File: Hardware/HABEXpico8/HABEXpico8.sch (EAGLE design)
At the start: 121 parts, among them IC1 LT1763CS8-3.3, Q1 2.5A/30V, SW1 SKQGADE010, SW2 SKQGADE010, U1 LTC3106, U2 EVA-8M, U3 STM32L011G4, U4 SI4464, U5 USB-C_R/A_HYBRID_RCPT, U6 FT232RL, U7 3.3V, X1 BU-SMA-V, X2 BU-SMA-V, X3 BU-SMA-V, X4 BU-SMA-V, X5 JTI_ANTENNA-1575AT43A40, X6 C-GRID-04-70553, X7 C-GRID-02-70553, X8 30MHZ 402F3001XIAR, X9 BU-SMA-V, Y1 ABS07-120-32.768KHZ-T, Y2 ABS07-120-32.768KHZ-T

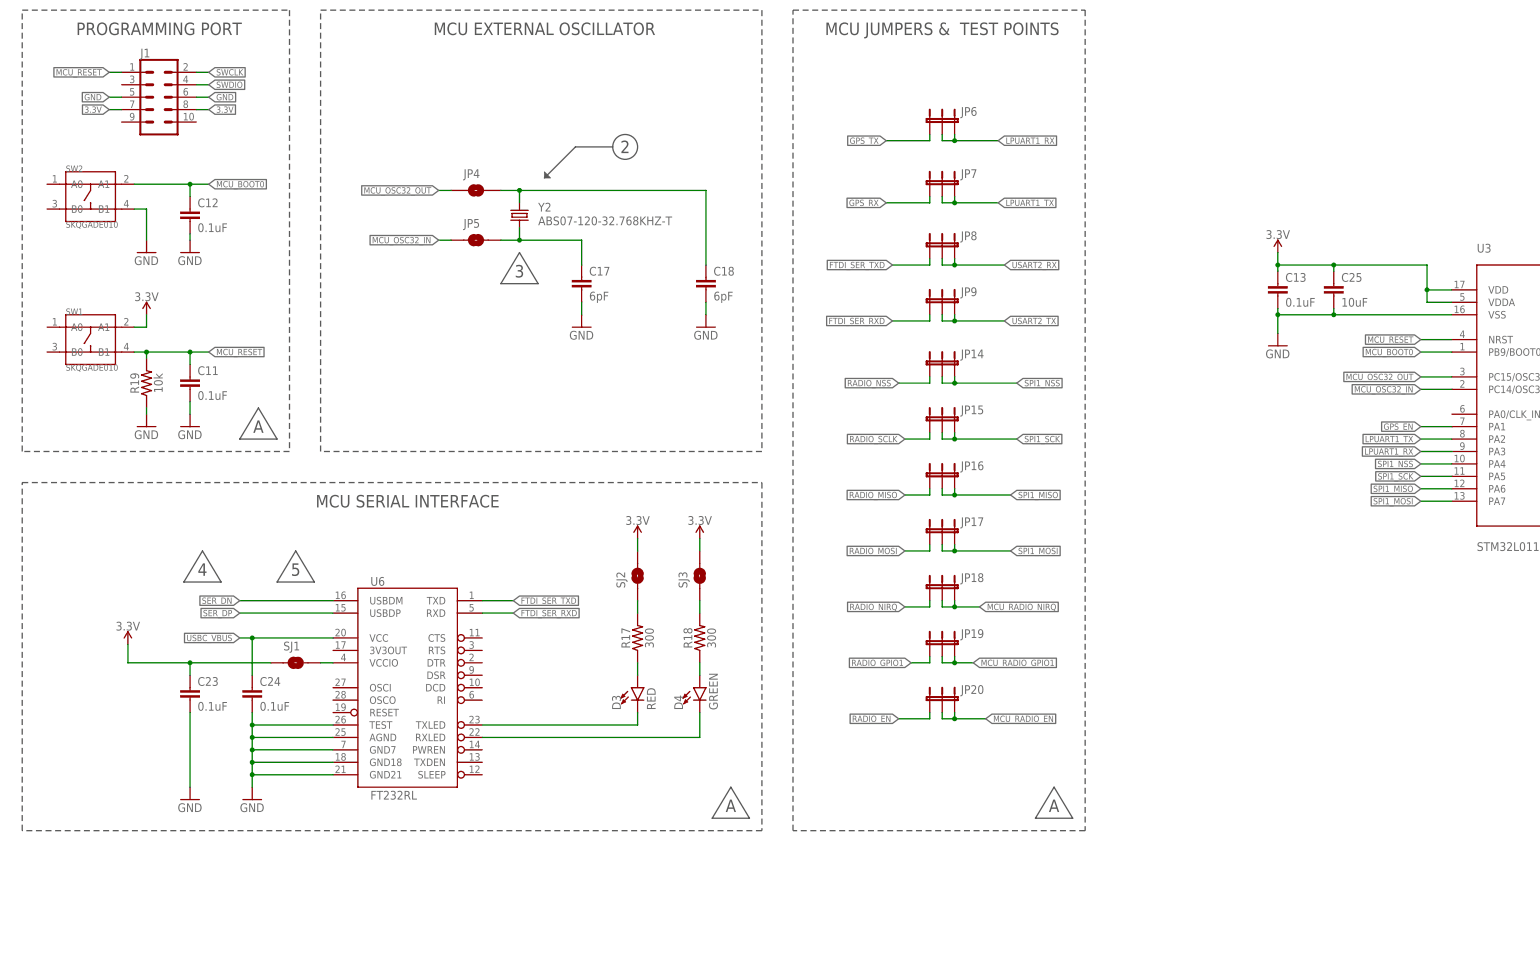
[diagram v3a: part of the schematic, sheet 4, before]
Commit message: Added BOM, updated board/schematic files
Added BOM, updated board/schematic files
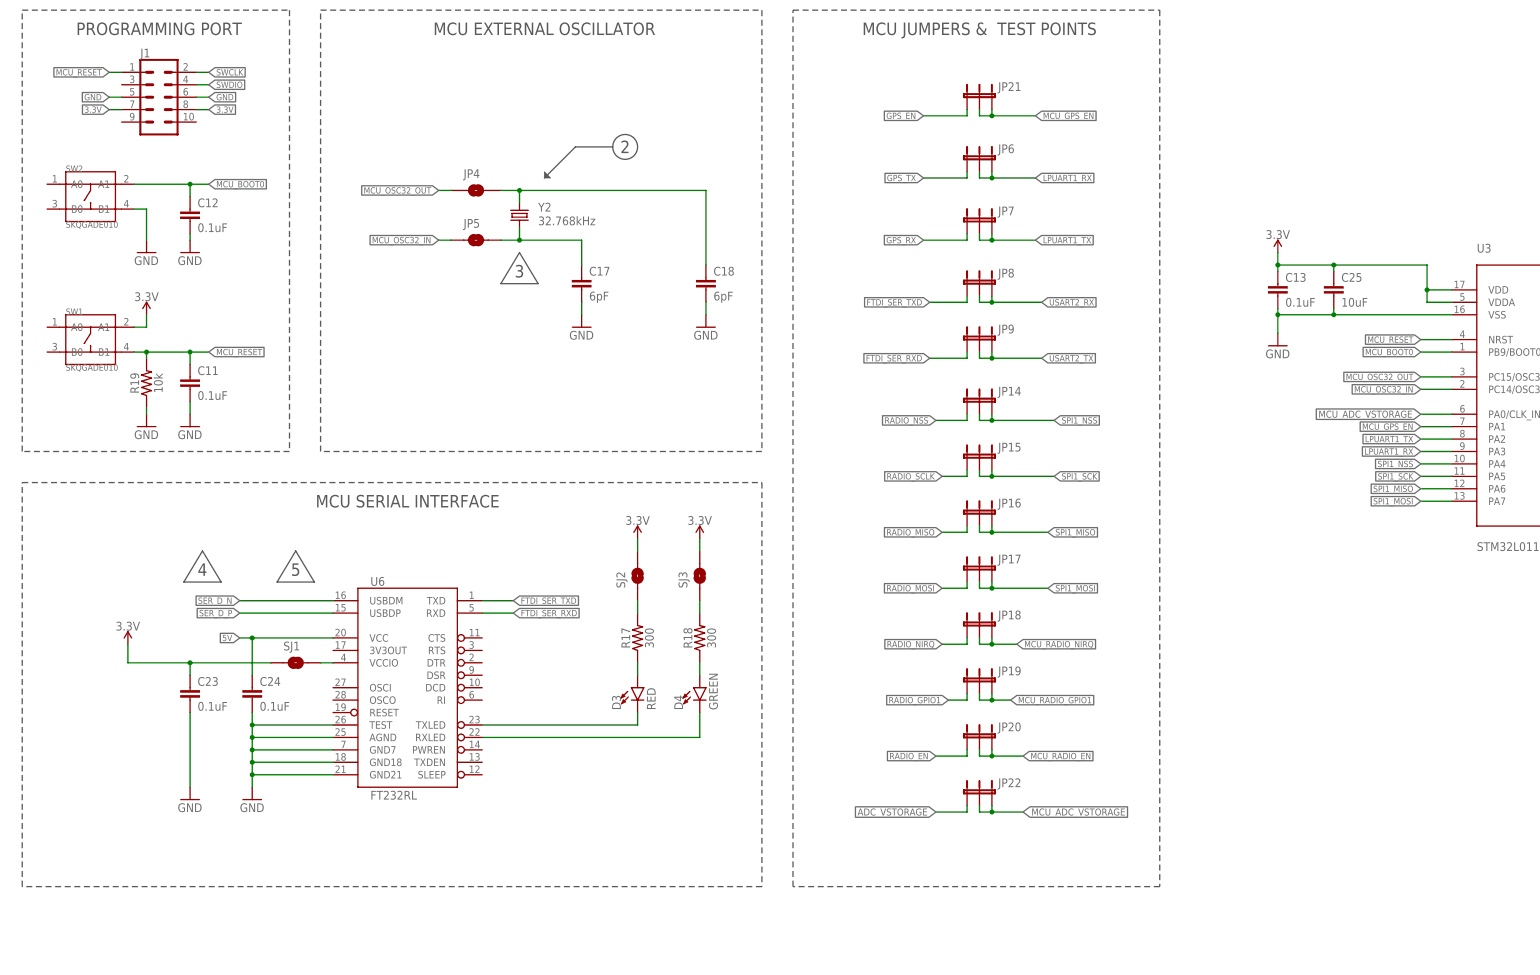
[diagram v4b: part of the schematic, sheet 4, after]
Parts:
- added JP21, JP22: JUMPER-3PTH, SparkFun-Retired:JUMPER-3PTH
- R1, R9: value 2.21M -> 1M
- R10, R2: value 1.33M -> 1M
- R14, R15: value 5.1k 10% -> 5.1K
- R3: value 10M -> 1M
- Y1, Y2: value ABS07-120-32.768KHZ-T -> 32.768kHz
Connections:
- net GPS_USB_DM renamed GPS_USB_N
- net GPS_USB_DP renamed GPS_USB_P
- net SER_DN renamed SER_D_N
- net SER_DP renamed SER_D_P
- new net ADC_VSTORAGE: JP22.1, R10.2, R9.1
- new net MCU_GPS_EN: JP21.2, JP21.3, U3.PA1
- net 5V: now also C24.1, U6.VCC
- net GPS_EN: now also JP21.1; no longer U3.PA1
- net MCU_ADC_VSTORAGE: now also JP22.2, JP22.3, U3.PA0/CLK_IN; no longer R10.2, R9.1
- net N$15: now also R16.1; no longer R13.1
- net N$16: now also R13.1; no longer R16.1
- net USBC_DN: now also CR2.I/O2_2; no longer CR2.I/O1_2
- net USBC_DP: now also CR2.I/O1_2; no longer CR2.I/O2_2
- net USBC_VBUS: no longer C24.1, U6.VCC
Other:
- note added: "1. BOARD DESIGN FOR PROGRAMMING, TESTING, AND QUALIFYING DEVICES NOTES: THIS PAGE"
- note added: "3.3V REGULATOR"
- note removed: "5V REGULATOR"
- note removed: "SUPPORT HARDWARE, NOT FOR FLIGHT 1. BOARD DESIGN FOR PROGRAMMING, TESTING, AND QUALIFYING DEVICES NOTES: THIS PAGE"
- moved on the sheet: JP14, JP15, JP16, JP17, JP18, JP19, JP20, JP6, JP7, JP8, JP9, R13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

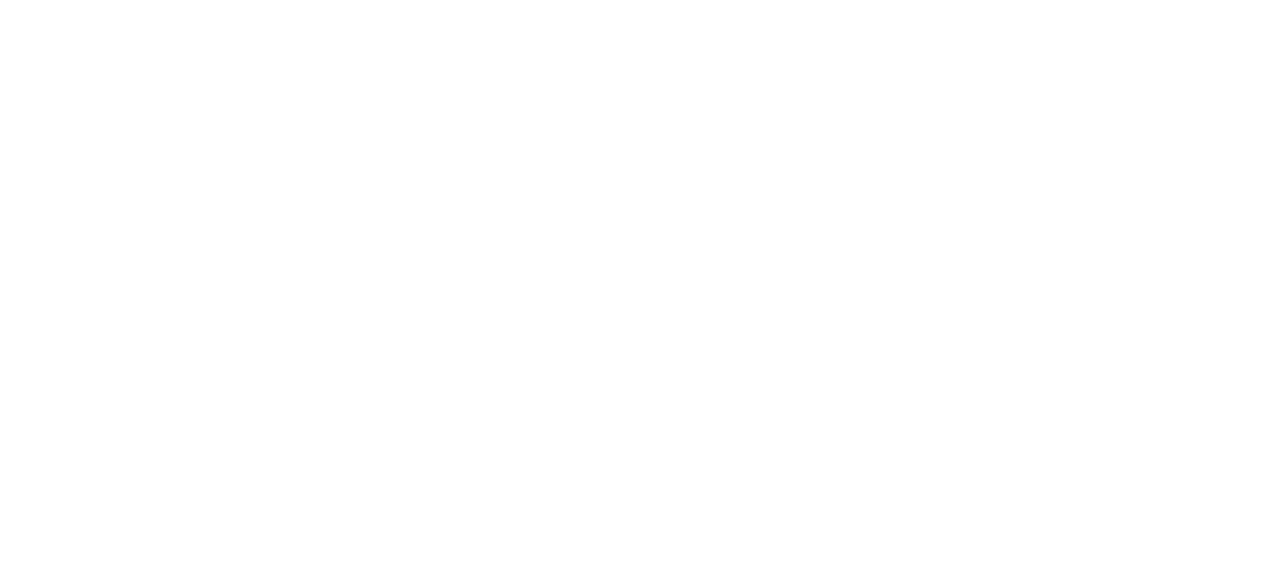
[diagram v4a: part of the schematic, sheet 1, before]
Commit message: Updated project to use the new stm32l0xx-hal
Updated project to use the new stm32l0xx-hal
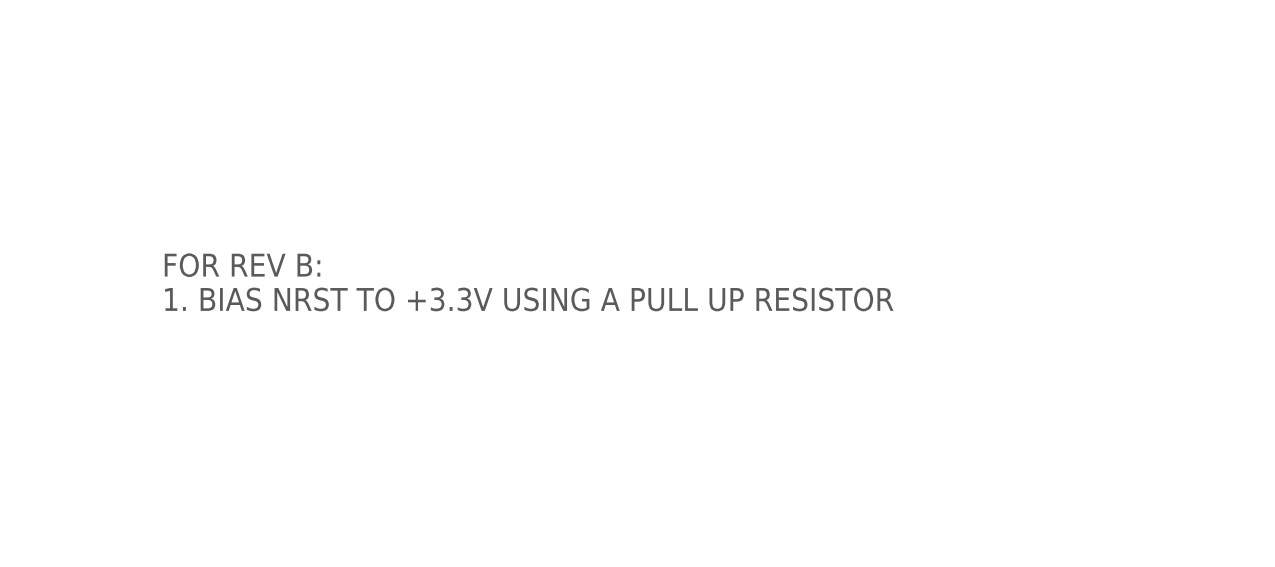
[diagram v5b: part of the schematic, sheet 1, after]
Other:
- note added: "FOR REV B: 1. BIAS NRST TO +3.3V USING A PULL UP RESISTOR"
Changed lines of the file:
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@@
 <?xml version="1.0" encoding="utf-8"?>
 <!DOCTYPE eagle SYSTEM "eagle.dtd">
-<eagle version="9.1.2">
+<eagle version="9.1.3">
 <drawing>
 <settings>
@@
 <setting verticaltext="up"/>
 </settings>
-<grid distance="0.05" unitdist="inch" unit="inch" style="dots" multiple="1" display="yes" altdistance="0.01" altunitdist="inch" altunit="inch"/>
+<grid distance="0.1" unitdist="inch" unit="inch" style="lines" multiple="1" display="no" altdistance="0.01" altunitdist="inch" altunit="inch"/>
 <layers>
-<layer number="1" name="Top" color="4" fill="1" visible="yes" active="no"/>
-<layer number="2" name="Route2" color="1" fill="3" visible="yes" active="no"/>
-<layer number="3" name="Route3" color="4" fill="3" visible="yes" active="no"/>
-<layer number="4" name="Route4" color="1" fill="4" visible="yes" active="no"/>
-<layer number="5" name="Route5" color="4" fill="4" visible="yes" active="no"/>
-<layer number="6" name="Route6" color="1" fill="8" visible="yes" active="no"/>
-<layer number="7" name="Route7" color="4" fill="8" visible="yes" active="no"/>
-<layer number="8" name="Route8" color="1" fill="2" visible="yes" active="no"/>
-<layer number="9" name="Route9" color="4" fill="2" visible="yes" active="no"/>
-<layer number="10" name="Route10" color="1" fill="7" visible="yes" active="no"/>
-<layer number="11" name="Route11" color="4" fill="7" visible="yes" active="no"/>
-<layer number="12" name="Route12" color="1" fill="5" visible="yes" active="no"/>
-<layer number="13" name="Route13" color="4" fill="5" visible="yes" active="no"/>
-<layer number="14" name="Route14" color="1" fill="6" visible="yes" active="no"/>
-<layer number="15" name="Route15" color="4" fill="6" visible="yes" active="no"/>
-<layer number="16" name="Bottom" color="1" fill="1" visible="yes" active="no"/>
-<layer number="17" name="Pads" color="2" fill="1" visible="yes" active="no"/>
-<layer number="18" name="Vias" color="2" fill="1" visible="yes" active="no"/>
-<layer number="19" name="Unrouted" color="6" fill="1" visible="yes" active="no"/>
-<layer number="20" name="Dimension" color="24" fill="1" visible="yes" active="no"/>
-<layer number="21" name="tPlace" color="7" fill="1" visible="yes" active="no"/>
-<layer number="22" name="bPlace" color="7" fill="1" visible="yes" active="no"/>
-<layer number="23" name="tOrigins" color="15" fill="1" visible="yes" active="no"/>
-<layer number="24" name="bOrigins" color="15" fill="1" visible="yes" active="no"/>
-<layer number="25" name="tNames" color="7" fill="1" visible="yes" active="no"/>
-<layer number="26" name="bNames" color="7" fill="1" visible="yes" active="no"/>
-<layer number="27" name="tValues" color="7" fill="1" visible="yes" active="no"/>
-<layer number="28" name="bValues" color="7" fill="1" visible="yes" active="no"/>
+<layer number="1" name="Top" color="4" fill="1" visible="no" active="no"/>
+<layer number="2" name="Route2" color="1" fill="3" visible="no" active="no"/>
+<layer number="3" name="Route3" color="4" fill="3" visible="no" active="no"/>
+<layer number="4" name="Route4" color="1" fill="4" visible="no" active="no"/>
+<layer number="5" name="Route5" color="4" fill="4" visible="no" active="no"/>
+<layer number="6" name="Route6" color="1" fill="8" visible="no" active="no"/>
+<layer number="7" name="Route7" color="4" fill="8" visible="no" active="no"/>
+<layer number="8" name="Route8" color="1" fill="2" visible="no" active="no"/>
+<layer number="9" name="Route9" color="4" fill="2" visible="no" active="no"/>
+<layer number="10" name="Route10" color="1" fill="7" visible="no" active="no"/>
+<layer number="11" name="Route11" color="4" fill="7" visible="no" active="no"/>
+<layer number="12" name="Route12" color="1" fill="5" visible="no" active="no"/>
+<layer number="13" name="Route13" color="4" fill="5" visible="no" active="no"/>
+<layer number="14" name="Route14" color="1" fill="6" visible="no" active="no"/>
+<layer number="15" name="Route15" color="4" fill="6" visible="no" active="no"/>
+<layer number="16" name="Bottom" color="1" fill="1" visible="no" active="no"/>
+<layer number="17" name="Pads" color="2" fill="1" visible="no" active="no"/>
+<layer number="18" name="Vias" color="2" fill="1" visible="no" active="no"/>
+<layer number="19" name="Unrouted" color="6" fill="1" visible="no" active="no"/>
+<layer number="20" name="Dimension" color="24" fill="1" visible="no" active="no"/>
+<layer number="21" name="tPlace" color="7" fill="1" visible="no" active="no"/>
+<layer number="22" name="bPlace" color="7" fill="1" visible="no" active="no"/>
+<layer number="23" name="tOrigins" color="15" fill="1" visible="no" active="no"/>
+<layer number="24" name="bOrigins" color="15" fill="1" visible="no" active="no"/>
+<layer number="25" name="tNames" color="7" fill="1" visible="no" active="no"/>
+<layer number="26" name="bNames" color="7" fill="1" visible="no" active="no"/>
+<layer number="27" name="tValues" color="7" fill="1" visible="no" active="no"/>
+<layer number="28" name="bValues" color="7" fill="1" visible="no" active="no"/>
 <layer number="29" name="tStop" color="7" fill="3" visible="no" active="no"/>
 <layer number="30" name="bStop" color="7" fill="6" visible="no" active="no"/>
@@
 <layer number="35" name="tGlue" color="7" fill="4" visible="no" active="no"/>
 <layer number="36" name="bGlue" color="7" fill="5" visible="no" active="no"/>
-<layer number="37" name="tTest" color="7" fill="1" visible="yes" active="no"/>
-<layer number="38" name="bTest" color="7" fill="1" visible="yes" active="no"/>
+<layer number="37" name="tTest" color="7" fill="1" visible="no" active="no"/>
+<layer number="38" name="bTest" color="7" fill="1" visible="no" active="no"/>
 <layer number="39" name="tKeepout" color="4" fill="11" visible="no" active="no"/>
 <layer number="40" name="bKeepout" color="1" fill="11" visible="no" active="no"/>
@@
 <layer number="44" name="Drills" color="7" fill="1" visible="no" active="no"/>
 <layer number="45" name="Holes" color="7" fill="1" visible="no" active="no"/>
-<layer number="46" name="Milling" color="3" fill="1" visible="yes" active="no"/>
-<layer number="47" name="Measures" color="7" fill="1" visible="yes" active="no"/>
-<layer number="48" name="Document" color="7" fill="1" visible="yes" active="no"/>
-<layer number="49" name="Reference" color="7" fill="1" visible="yes" active="no"/>
-<layer number="50" name="dxf" color="7" fill="1" visible="yes" active="no"/>
-<layer number="51" name="tDocu" color="7" fill="1" visible="yes" active="no"/>
-<layer number="52" name="bDocu" color="7" fill="1" visible="yes" active="no"/>
-<layer number="53" name="tGND_GNDA" color="7" fill="9" visible="yes" active="no"/>
-<layer number="54" name="bGND_GNDA" color="1" fill="9" visible="yes" active="no"/>
-<layer number="56" name="wert" color="7" fill="1" visible="yes" active="no"/>
-<layer number="57" name="tCAD" color="7" fill="1" visible="yes" active="no"/>
-<layer number="59" name="tCarbon" color="7" fill="1" visible="yes" active="no"/>
-<layer number="60" name="bCarbon" color="7" fill="1" visible="yes" active="no"/>
+<layer number="46" name="Milling" color="3" fill="1" visible="no" active="no"/>
+<layer number="47" name="Measures" color="7" fill="1" visible="no" active="no"/>
+<layer number="48" name="Document" color="7" fill="1" visible="no" active="no"/>
+<layer number="49" name="Reference" color="7" fill="1" visible="no" active="no"/>
+<layer number="50" name="dxf" color="7" fill="1" visible="no" active="no"/>
+<layer number="51" name="tDocu" color="7" fill="1" visible="no" active="no"/>
+<layer number="52" name="bDocu" color="7" fill="1" visible="no" active="no"/>
+<layer number="53" name="tGND_GNDA" color="7" fill="9" visible="no" active="no"/>
+<layer number="54" name="bGND_GNDA" color="1" fill="9" visible="no" active="no"/>
+<layer number="56" name="wert" color="7" fill="1" visible="no" active="no"/>
+<layer number="57" name="tCAD" color="7" fill="1" visible="no" active="no"/>
+<layer number="59" name="tCarbon" color="7" fill="1" visible="no" active="no"/>
+<layer number="60" name="bCarbon" color="7" fill="1" visible="no" active="no"/>
 <layer number="90" name="Modules" color="5" fill="1" visible="yes" active="yes"/>
 <layer number="91" name="Nets" color="2" fill="1" visible="yes" active="yes"/>
@@
 <wire x1="26.67" y1="64.77" x2="26.67" y2="140.97" width="0.1524" layer="97" style="shortdash"/>
 <text x="96.52" y="134.62" size="3.81" layer="97" align="bottom-center">GSE</text>
+<text x="223.52" y="148.59" size="2.54" layer="97">FOR REV B:
+1. BIAS NRST TO +3.3V USING A PULL UP RESISTOR</text>
 </plain>
 <instances>
